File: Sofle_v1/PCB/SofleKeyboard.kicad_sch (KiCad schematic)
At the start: 96 parts, among them J1 LED, J2 4PIN, J3 OLED, P1 i2c_pin, P2 i2c_pin, SW1 SW_PUSH, SW10 SW_PUSH, SW11 SW_PUSH, SW12 SW_PUSH, SW13 SW_PUSH, SW14 SW_PUSH, SW15 SW_PUSH, SW16 SW_PUSH, SW17 SW_PUSH, SW18 SW_PUSH, SW19 SW_PUSH, SW2 SW_PUSH, SW20 SW_PUSH, SW21 SW_PUSH, SW22 SW_PUSH, SW23 SW_PUSH, SW24 SW_PUSH, SW25 Rotary_Encoder_Switch, SW26 SW_PUSH, SW27 SW_PUSH, SW28 SW_PUSH, SW29 SW_PUSH, SW3 SW_PUSH, SW30 SW_PUSH, SW31 SW_PUSH, SW32 SW_PUSH, SW33 SW_PUSH, SW34 SW_PUSH, SW35 SW_PUSH, SW4 SW_PUSH, SW5 SW_PUSH, SW6 SW_PUSH, SW7 SW_PUSH, SW8 SW_PUSH, SW9 SW_PUSH, U1 ProMicro

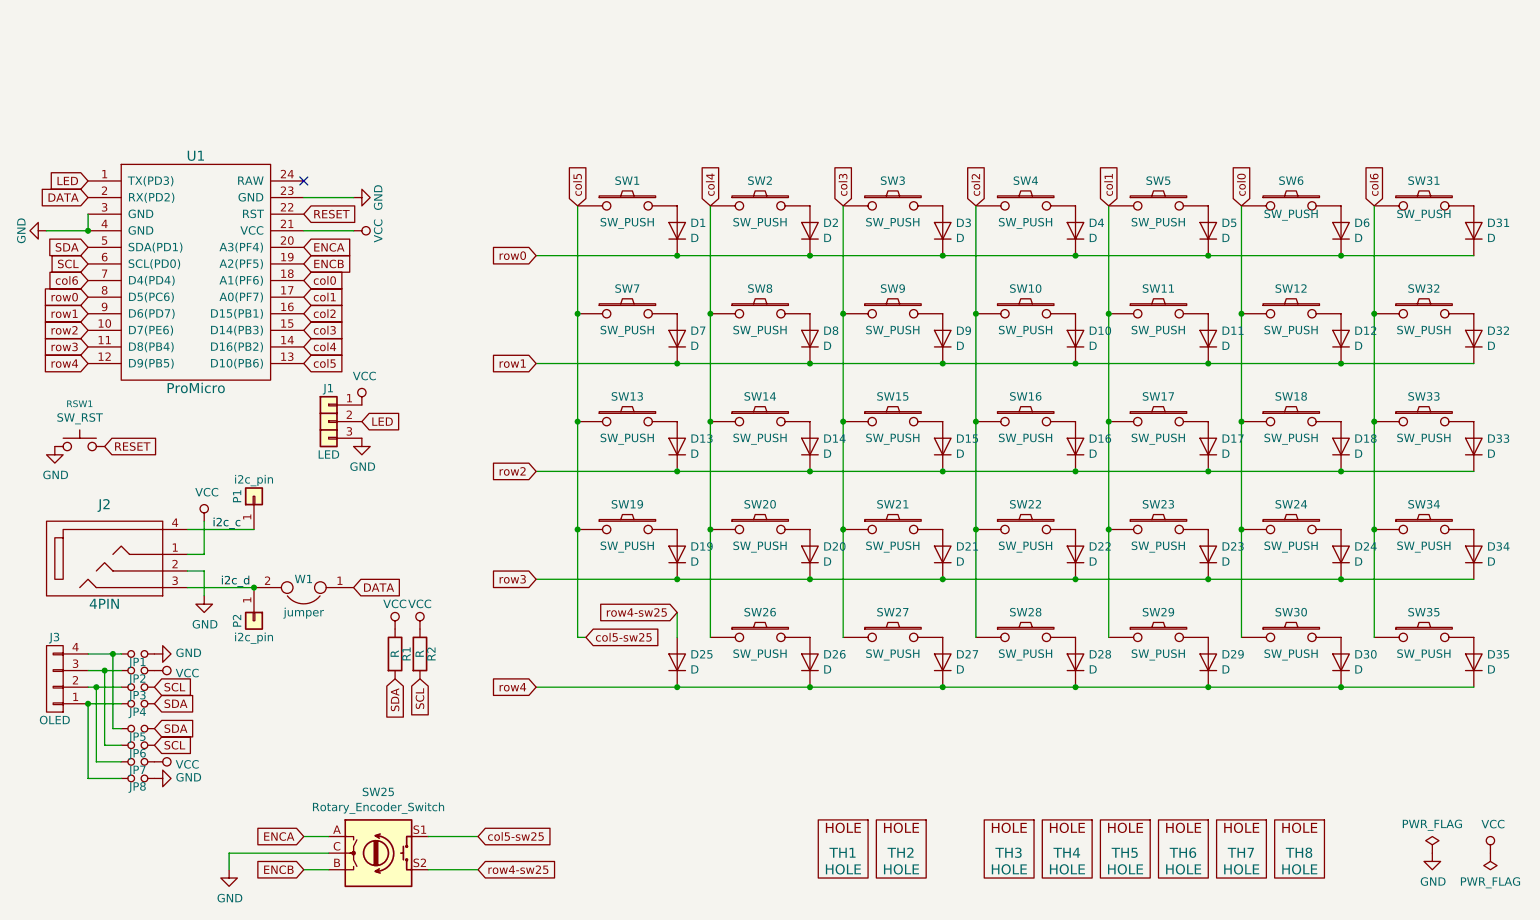
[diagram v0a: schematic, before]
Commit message: Moved TRRS + battery connector.
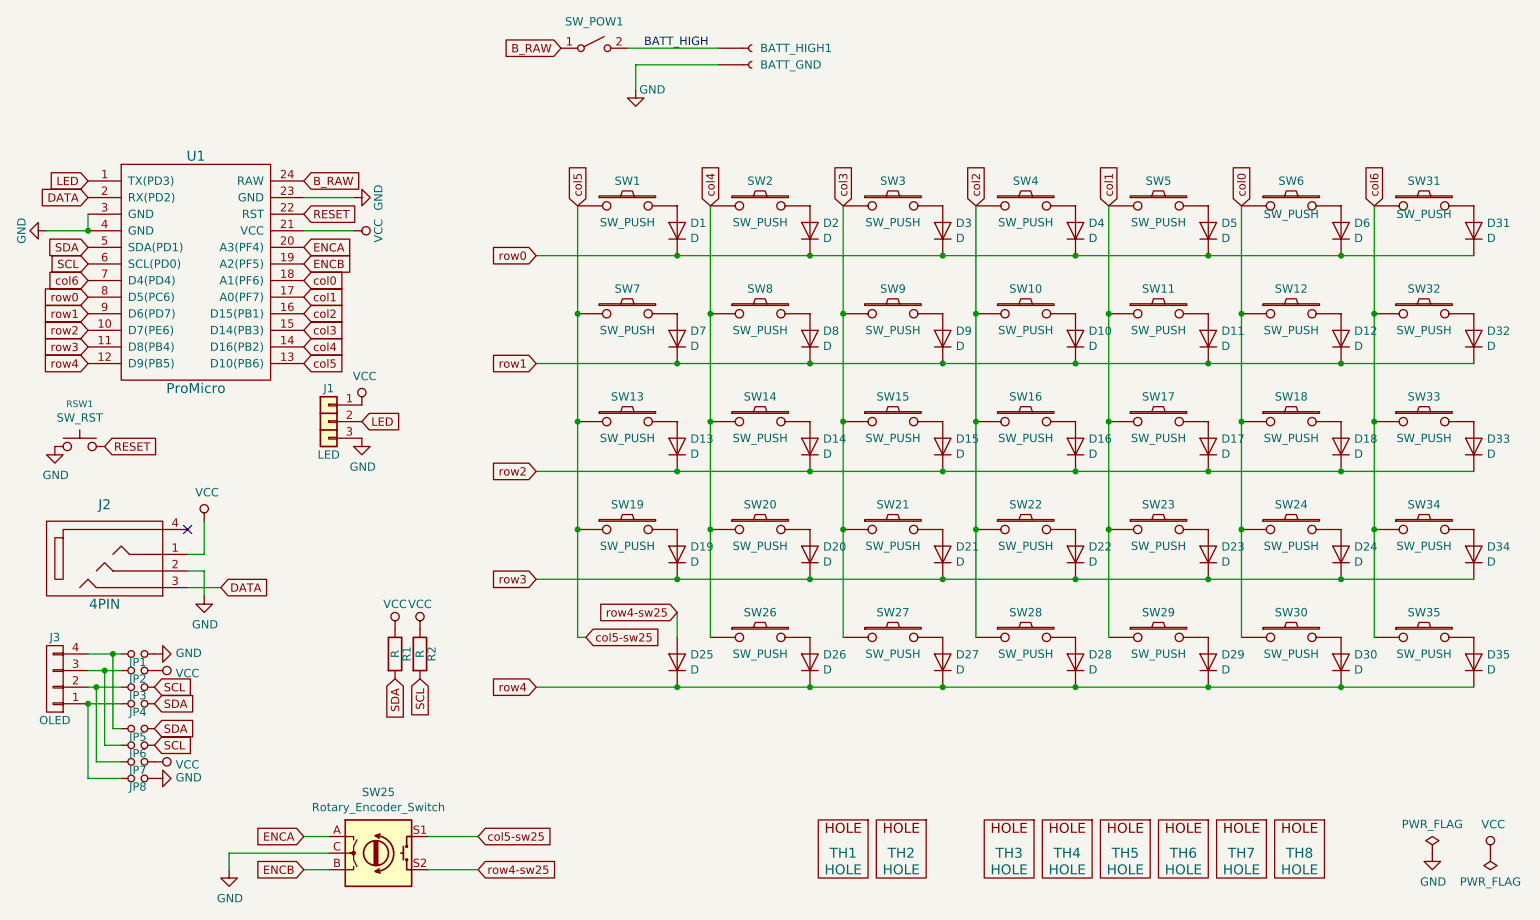
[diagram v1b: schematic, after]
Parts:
- removed P1, P2: i2c_pin, SofleKeyboard-footprint:1pin_conn, symbol SofleKeyboard-rescue:i2c_pin-Lily58-cache-Lily58_Pro-rescue
- removed W1: jumper, SofleKeyboard-footprint:jumper_data, symbol Device:Jumper
- added BATT_HIGH1: BATT_GND, SofleKeyboard-footprint:Sofle_JST_PH_S2B-PH-K_1x02_P2.00mm_Horizontal, symbol SofleKeyboard:Conn_01x02_Female
- added SW_POW1: POWER_SWITCH, SofleKeyboard-footprint:Sofle_SW_SPDT_PCM12, symbol SofleKeyboard:Sofle_SW_SPST
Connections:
- net i2c_d is gone; now on net DATA: J2.3
- net GND: now also BATT_HIGH1.2 (Pin_2)
- net B_RAW: now reaches U1.24 (RAW)
- net B_RAW: now also SW_POW1.1 (A)
- net i2c_c: no longer names the net of J2.4
- new net BATT_HIGH: BATT_HIGH1.1 (Pin_1), SW_POW1.2 (B)
